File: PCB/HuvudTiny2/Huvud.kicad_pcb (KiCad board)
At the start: 4 copper layers, 42 x 42 mm, 107 parts, among them J1 MOLEX Micro Fit 2x3, J10 FAN0, J2 DBG, J3 THERM, J4 FAN1, J5 FAN2, J6 Heater, J7 Endstop, J8 THERM, J9 STEPPER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

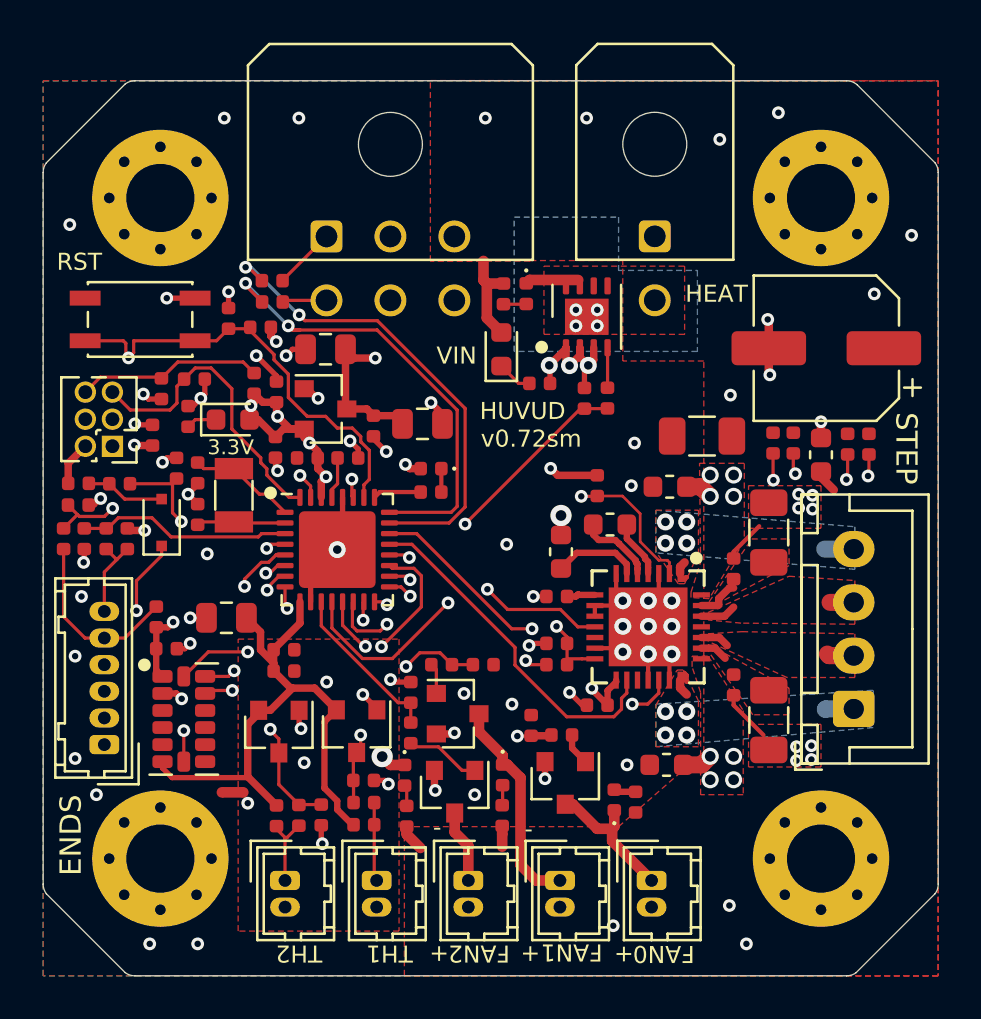
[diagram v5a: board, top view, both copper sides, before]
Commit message: LDO power supply from 24V.
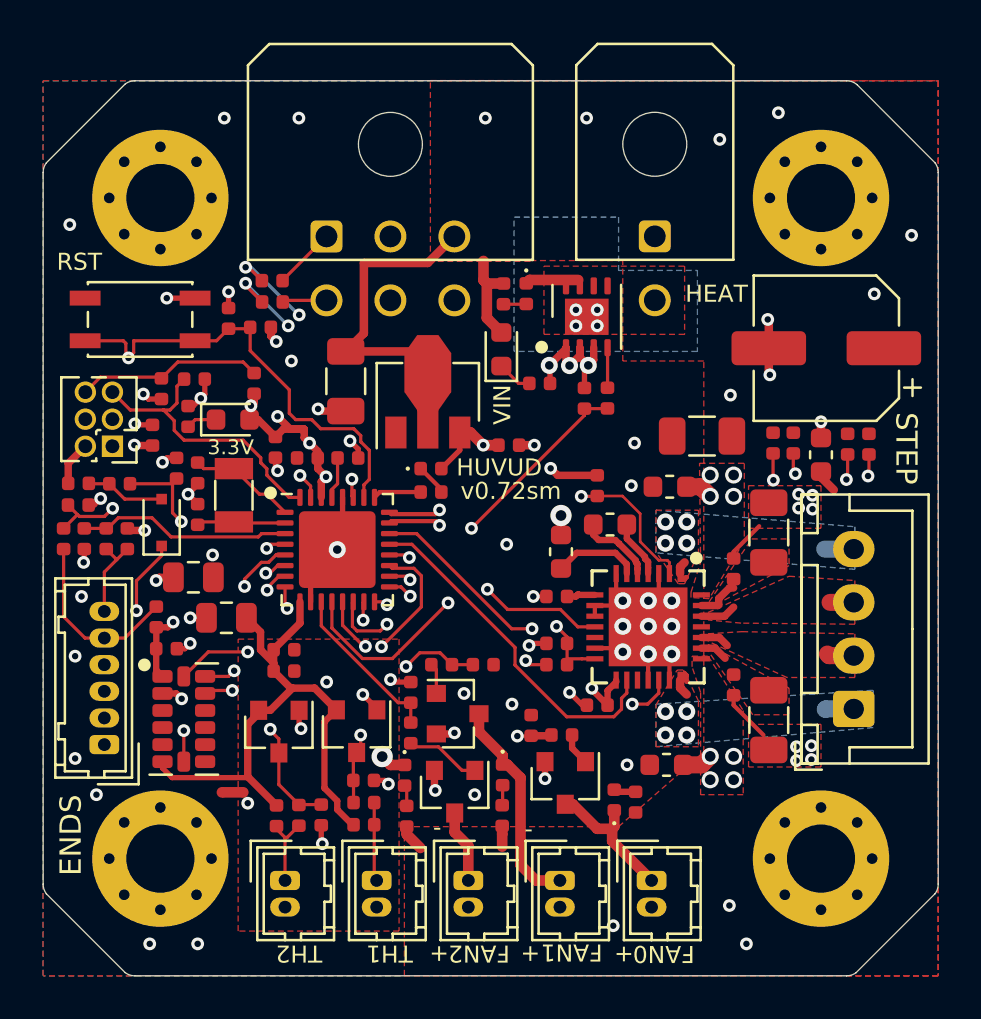
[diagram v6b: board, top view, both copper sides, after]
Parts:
- removed C32: 22uF, Capacitor_SMD:C_0805_2012Metric
- removed C35: 4.7uF, Capacitor_SMD:C_0402_1005Metric
- added C14: 10uF/35V, Capacitor_SMD:C_1206_3216Metric, F.Cu at (196.2, 114.1)
- R20, R3: value 470 -> 1k
- U4: value XC6206PxxxMR -> HT7533-1-SOT89; footprint Package_TO_SOT_SMD:SOT-23 -> Package_TO_SOT_SMD:SOT-89-3
- moved C15 12.4 mm to (189.1, 123.3), turned to 0 degrees
- moved C33 11.2 mm to (203.8, 117.1), turned to 180 degrees
- moved U4 4.81 mm to (200.1, 115.0), turned to 90 degrees
- turned D5 to 0 degrees
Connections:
- U4 pad 2: +3V3 -> ST_VS
- U4 pad 3: +5V -> +3V3
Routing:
- net ST_VS: track 30.0 -> 43.2 mm
- net +5V: track 14.0 -> 2.42 mm
- net GND: track 54.5 -> 50.9 mm, vias 66 -> 64
- net USBD+: track 21.7 -> 19.3 mm, vias 2 -> 3
- net USBD-: track 22.6 -> 20.7 mm, vias 2 -> 3
- net +3V3: track 33.3 -> 34.8 mm
- net SWDIO: track 14.4 -> 13.4 mm
- net GNDA: vias 7 -> 6

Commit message: Re work power supply added 5V stage: 24v->5V->3.3V
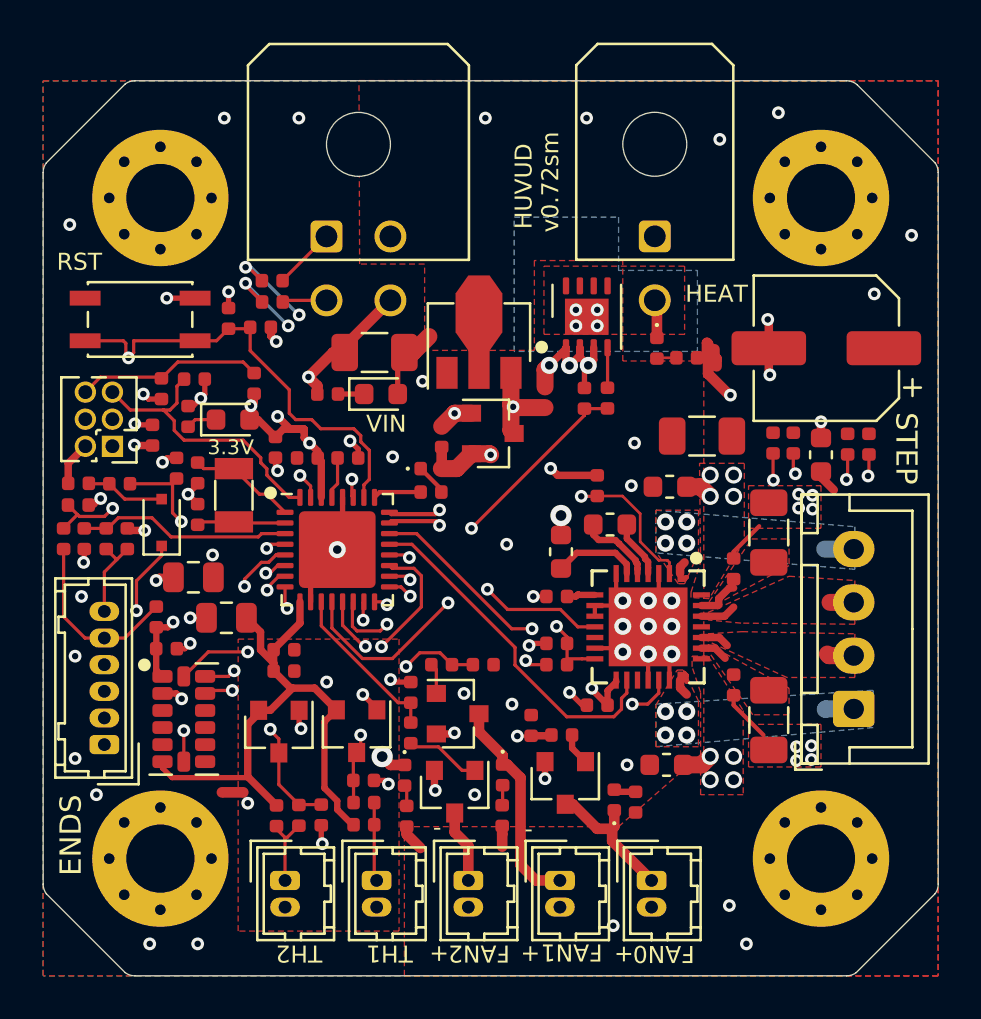
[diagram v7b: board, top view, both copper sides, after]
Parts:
- added C17: 4.7uF, Capacitor_SMD:C_0402_1005Metric, F.Cu at (200.7, 116.7)
- added U5: XC6206PxxxMR, Package_TO_SOT_SMD:SOT-23, F.Cu at (203.1, 116.5)
- J1: value MOLEX Micro Fit 2x3 -> MOLEX Micro Fit 2x2; footprint Connector_Molex:Molex_Micro-Fit_3.0_43045-0600_2x03_P3.00mm_Horizontal -> Connector_Molex:Molex_Micro-Fit_3.0_43045-0400_2x02_P3.00mm_Horizontal
- U4: value HT7533-1-SOT89 -> HT7550-1-SOT89
- moved R11 9.96 mm to (195.3, 114.7), turned to 180 degrees
- moved R15 9.11 mm to (212.2, 113.0), turned to 180 degrees
- moved D3 6.64 mm to (210.8, 112.5)
- moved D6 6.03 mm to (197.8, 114.7), turned to 0 degrees
- moved U4 3.69 mm to (202.4, 112.2)
- moved C33 2.82 mm to (205.6, 114.8), turned to -90 degrees
- moved C14 1.91 mm to (197.6, 112.8), turned to 0 degrees
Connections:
- C33 pad 2: +3V3 -> +5V
- J1 pad 2: +5V -> ST_VS
- J1 pad 3: ST_VS -> /D+
- J1 pad 4: /D+ -> GND
- U4 pad 3: +3V3 -> +5V
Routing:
- net +5V: track 2.42 -> 20.6 mm, vias 1 -> 2
- net ST_VS: track 43.2 -> 34.3 mm
- net GND: track 50.9 -> 57.3 mm, vias 64 -> 65
- net Net-(D3-Pad1): track 2.50 -> 1.81 mm
- net +3V3: track 34.8 -> 34.1 mm, vias 12 -> 11

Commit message: Resolve DRC warnings.
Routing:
- net +3V3: track 34.1 -> 33.2 mm, vias 11 -> 10
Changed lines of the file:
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@@
   )
   (footprint "Resistor_SMD:R_0402_1005Metric" (layer "F.Cu")
-    (at 187.31 125.16 -90)
+    (at 187.3 125.2 -90)
     (descr "Resistor SMD 0402 (1005 Metric), square (rectangular) end terminal, IPC_7351 nominal, (Body size source: http://www.tortai-tech.com/upload/download/2011102023233369053.pdf), generated with kicad-footprint-generator")
     (tags "resistor")
@@
   (segment (start 186.7674 121.1007) (end 186.0457 121.1007) (width 0.35) (layer "F.Cu") (net 8))
   (segment (start 191.75 115.25) (end 191.75 115.8375) (width 0.35) (layer "F.Cu") (net 8))
-  (segment (start 192.95 115.7) (end 193 115.75) (width 0.35) (layer "F.Cu") (net 8))
   (segment (start 208.8878 128.2122) (end 208.485 128.615) (width 0.3) (layer "F.Cu") (net 8))
   (segment (start 200.7 118.185) (end 200.685 118.2) (width 0.5) (layer "F.Cu") (net 8))
@@
   (segment (start 183.175 118.89) (end 183.175 117.955) (width 0.35) (layer "F.Cu") (net 8))
   (segment (start 208.8878 128.1248) (end 208.8878 128.2122) (width 0.3) (layer "F.Cu") (net 8))
-  (segment (start 193.6 116.35) (end 193 115.75) (width 0.35) (layer "F.Cu") (net 8))
   (segment (start 207.7484 128.5062) (end 207.7484 128.5634) (width 0.3) (layer "F.Cu") (net 8))
   (segment (start 187.31 126.645) (end 187.305 126.65) (width 0.3) (layer "F.Cu") (net 8))
@@
   (via (at 203 117.55) (size 0.6) (drill 0.3) (layers "F.Cu" "B.Cu") (net 8))
   (via (at 188.1 125.4) (size 0.6) (drill 0.3) (layers "F.Cu" "B.Cu") (net 8))
-  (via (at 193 115.75) (size 0.6) (drill 0.3) (layers "F.Cu" "B.Cu") (net 8))
   (via (at 186.2797 117.095) (size 0.6) (drill 0.3) (layers "F.Cu" "B.Cu") (net 8))
   (via (at 191.75 115.25) (size 0.6) (drill 0.3) (layers "F.Cu" "B.Cu") (net 8))
